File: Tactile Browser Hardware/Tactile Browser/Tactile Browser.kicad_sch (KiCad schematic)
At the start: 78 parts, among them SW1 SW_Push, SW10 SW_Push, SW11 SW_Push, SW12 SW_Push, SW13 SW_Push, SW14 SW_Push, SW15 SW_Push, SW16 SW_Push, SW17 SW_Push, SW18 SW_Push, SW19 SW_Push, SW2 SW_Push, SW20 SW_Push, SW3 SW_Push, SW4 SW_Push, SW5 SW_Push, SW6 SW_Push, SW7 SW_Push, SW8 SW_Push, SW9 SW_Push

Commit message: I2C
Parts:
- added I2C_bus: Conn_01x02_Pin, symbol Connector:Conn_01x02_Pin
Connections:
- net SDA: now reaches A1.23 (A4)
- net SDA: now also I2C_bus.1 (Pin_1)
- net SCL: now reaches A1.24 (A5)
- net SCL: now also I2C_bus.2 (Pin_2)
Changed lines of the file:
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@@
 		)
 	)
+	(global_label "SCL"
+		(shape input)
+		(at 254 71.12 270)
+		(fields_autoplaced yes)
+		(effects
+			(font
+				(size 1.27 1.27)
+			)
+			(justify right)
+		)
+		(property "Intersheetrefs" "${INTERSHEET_REFS}"
+			(at 254 77.6128 90)
+			(effects
+				(font
+					(size 1.27 1.27)
+				)
+				(justify right)
+				(hide yes)
+			)
+		)
+	)
 	(global_label "S2_in1"
 		(shape input)
@@
 		)
 	)
+	(global_label "SDA"
+		(shape input)
+		(at 256.54 71.12 270)
+		(fields_autoplaced yes)
+		(effects
+			(font
+				(size 1.27 1.27)
+			)
+			(justify right)
+		)
+		(property "Intersheetrefs" "${INTERSHEET_REFS}"
+			(at 256.54 77.6733 90)
+			(effects
+				(font
+					(size 1.27 1.27)
+				)
+				(justify right)
+				(hide yes)
+			)
+		)
+	)
 	(global_label "12V"
 		(shape input)
@@
 		)
 	)
+	(global_label "SDA"
+		(shape input)
+		(at 275.59 237.49 0)
+		(fields_autoplaced yes)
+		(effects
+			(font
+				(size 1.27 1.27)
+			)
+			(justify left)
+		)
+		(property "Intersheetrefs" "${INTERSHEET_REFS}"
+			(at 282.1433 237.49 0)
+			(effects
+				(font
+					(size 1.27 1.27)
+				)
+				(justify left)
+				(hide yes)
+			)
+		)
+	)
 	(global_label "S18_out2"
 		(shape input)
@@
 		)
 	)
+	(global_label "SCL"
+		(shape input)
+		(at 275.59 240.03 0)
+		(fields_autoplaced yes)
+		(effects
+			(font
+				(size 1.27 1.27)
+			)
+			(justify left)
+		)
+		(property "Intersheetrefs" "${INTERSHEET_REFS}"
+			(at 282.0828 240.03 0)
+			(effects
+				(font
+					(size 1.27 1.27)
+				)
+				(justify left)
+				(hide yes)
+			)
+		)
+	)
 	(global_label "5V"
 		(shape input)
@@
 					(unit 1)
 				)
+			)
+		)
+	)
+	(symbol
+		(lib_id "Connector:Conn_01x02_Pin")
+		(at 256.54 66.04 270)
+		(unit 1)
+		(exclude_from_sim no)
+		(in_bom yes)
+		(on_board yes)
+		(dnp no)
+		(fields_autoplaced yes)
+		(property "Reference" "I2C_bus"
+			(at 257.81 65.4049 90)
+			(effects
+				(font
+					(size 1.27 1.27)
+				)
+				(justify left)
+			)
+		)
+		(property "Value" "Conn_01x02_Pin"
+			(at 257.81 67.9449 90)
+			(effects
+				(font
+					(size 1.27 1.27)
+				)
+				(justify left)
+			)
+		)
+		(property "Footprint" ""
+			(at 256.54 66.04 0)
+			(effects
+				(font
+					(size 1.27 1.27)
+				)
+				(hide yes)
+			)
+		)
+		(property "Datasheet" "~"
+			(at 256.54 66.04 0)
+			(effects
+				(font
+					(size 1.27 1.27)
+				)
+				(hide yes)
+			)
+		)
+		(property "Description" "Generic connector, single row, 01x02, script generated"
+			(at 256.54 66.04 0)
+			(effects
+				(font
+					(size 1.27 1.27)
+				)
+				(hide yes)
+			)
+		)
+		(pin "1"
+		)
+		(pin "2"
+		)
+		(instances
+			(project ""
+				(path "/2e399075-89ae-469c-893b-1284214b820d"
+					(reference "I2C_bus")
+					(unit 1)
+				)

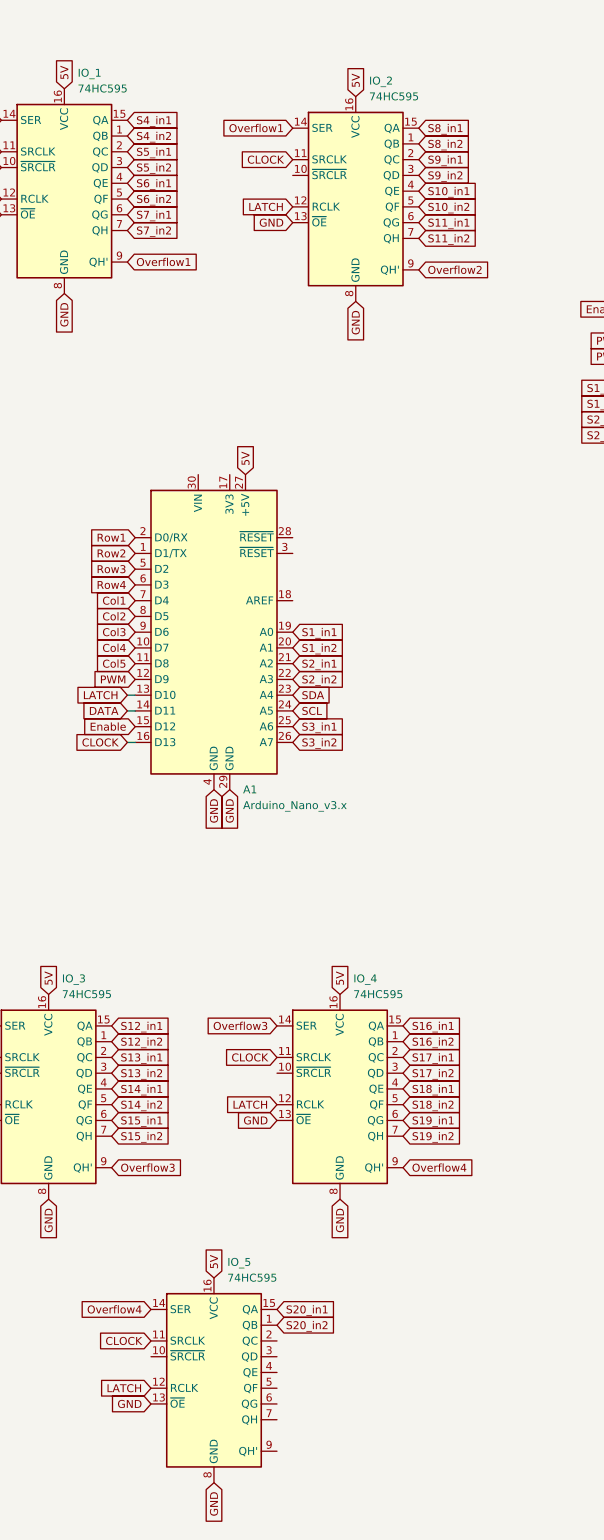
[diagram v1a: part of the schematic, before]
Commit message: moved all solenoids to 74hc595s
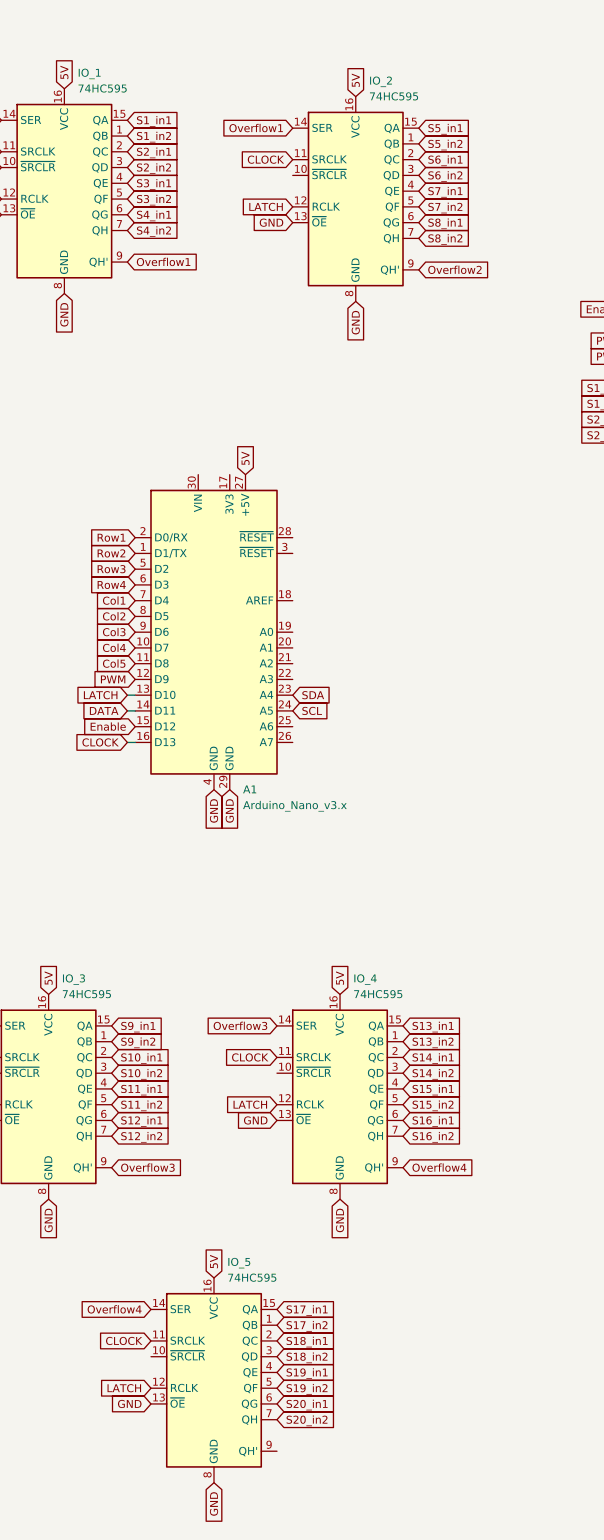
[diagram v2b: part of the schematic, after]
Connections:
- net S10_in1: now also IO_3.2 (QC); no longer IO_2.4 (QE)
- net S10_in2: now also IO_3.3 (QD); no longer IO_2.5 (QF)
- net S11_in1: now also IO_3.4 (QE); no longer IO_2.6 (QG)
- net S11_in2: now also IO_3.5 (QF); no longer IO_2.7 (QH)
- net S12_in1: now also IO_3.6 (QG); no longer IO_3.15 (QA)
- net S12_in2: now also IO_3.7 (QH); no longer IO_3.1 (QB)
- net S13_in1: now also IO_4.15 (QA); no longer IO_3.2 (QC)
- net S13_in2: now also IO_4.1 (QB); no longer IO_3.3 (QD)
- net S14_in1: now also IO_4.2 (QC); no longer IO_3.4 (QE)
- net S14_in2: now also IO_4.3 (QD); no longer IO_3.5 (QF)
- net S15_in1: now also IO_4.4 (QE); no longer IO_3.6 (QG)
- net S15_in2: now also IO_4.5 (QF); no longer IO_3.7 (QH)
- net S16_in1: now also IO_4.6 (QG); no longer IO_4.15 (QA)
- net S16_in2: now also IO_4.7 (QH); no longer IO_4.1 (QB)
- net S17_in1: now also IO_5.15 (QA); no longer IO_4.2 (QC)
- net S17_in2: now also IO_5.1 (QB); no longer IO_4.3 (QD)
- net S18_in1: now also IO_5.2 (QC); no longer IO_4.4 (QE)
- net S18_in2: now also IO_5.3 (QD); no longer IO_4.5 (QF)
- net S19_in1: now also IO_5.4 (QE); no longer IO_4.6 (QG)
- net S19_in2: now also IO_5.5 (QF); no longer IO_4.7 (QH)
- net S1_in1: now also IO_1.15 (QA); no longer A1.19 (A0)
- net S1_in2: now also IO_1.1 (QB); no longer A1.20 (A1)
- net S20_in1: now also IO_5.6 (QG); no longer IO_5.15 (QA)
- net S20_in2: now also IO_5.7 (QH); no longer IO_5.1 (QB)
- net S2_in1: now also IO_1.2 (QC); no longer A1.21 (A2)
- net S2_in2: now also IO_1.3 (QD); no longer A1.22 (A3)
- net S3_in1: now also IO_1.4 (QE); no longer A1.25 (A6)
- net S3_in2: now also IO_1.5 (QF); no longer A1.26 (A7)
- net S4_in1: now also IO_1.6 (QG); no longer IO_1.15 (QA)
- net S4_in2: now also IO_1.7 (QH); no longer IO_1.1 (QB)
- net S5_in1: now also IO_2.15 (QA); no longer IO_1.2 (QC)
- net S5_in2: now also IO_2.1 (QB); no longer IO_1.3 (QD)
- net S6_in1: now also IO_2.2 (QC); no longer IO_1.4 (QE)
- net S6_in2: now also IO_2.3 (QD); no longer IO_1.5 (QF)
- net S7_in1: now also IO_2.4 (QE); no longer IO_1.6 (QG)
- net S7_in2: now also IO_2.5 (QF); no longer IO_1.7 (QH)
- net S8_in1: now also IO_2.6 (QG); no longer IO_2.15 (QA)
- net S8_in2: now also IO_2.7 (QH); no longer IO_2.1 (QB)
- net S9_in1: now also IO_3.15 (QA); no longer IO_2.2 (QC)
- net S9_in2: now also IO_3.1 (QB); no longer IO_2.3 (QD)
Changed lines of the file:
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@@
 		)
 	)
-	(global_label "S8_in2"
+	(global_label "S5_in2"
 		(shape input)
 		(at 295.91 148.59 0)
@@
 		)
 	)
-	(global_label "S5_in2"
+	(global_label "S2_in2"
 		(shape input)
 		(at 248.92 152.4 0)
@@
 		)
 	)
-	(global_label "S11_in1"
+	(global_label "S8_in1"
 		(shape input)
 		(at 295.91 161.29 0)
@@
 		)
 		(property "Intersheetrefs" "${INTERSHEET_REFS}"
-			(at 306.4546 161.29 0)
+			(at 305.2451 161.29 0)
 			(effects
 				(font
@@
 		)
 	)
-	(global_label "S19_in1"
+	(global_label "S16_in1"
 		(shape input)
 		(at 293.37 306.07 0)
@@
 		)
 	)
-	(global_label "S12_in1"
+	(global_label "S9_in1"
 		(shape input)
 		(at 246.38 290.83 0)
@@
 		)
 		(property "Intersheetrefs" "${INTERSHEET_REFS}"
-			(at 256.9246 290.83 0)
+			(at 255.7151 290.83 0)
 			(effects
 				(font
@@
 		)
 	)
-	(global_label "S6_in2"
+	(global_label "S3_in2"
 		(shape input)
 		(at 248.92 157.48 0)
@@
 		)
 	)
-	(global_label "S14_in1"
+	(global_label "S11_in1"
 		(shape input)
 		(at 246.38 300.99 0)
@@
 		)
 	)
-	(global_label "S18_in2"
+	(global_label "S15_in2"
 		(shape input)
 		(at 293.37 303.53 0)
@@
 		)
 	)
-	(global_label "S20_in2"
+	(global_label "S17_in2"
 		(shape input)
 		(at 273.05 339.09 0)
@@
 		)
 	)
-	(global_label "S2_in2"
+	(global_label "S19_in2"
 		(shape input)
-		(at 275.59 234.95 0)
+		(at 273.05 349.25 0)
 		(fields_autoplaced yes)
 		(effects
@@
 		)
 		(property "Intersheetrefs" "${INTERSHEET_REFS}"
-			(at 284.9251 234.95 0)
+			(at 283.5946 349.25 0)
 			(effects
 				(font
@@
 		)
 	)
-	(global_label "S1_in1"
+	(global_label "S18_in1"
 		(shape input)
-		(at 275.59 227.33 0)
+		(at 273.05 341.63 0)
 		(fields_autoplaced yes)
 		(effects
@@
 		)
 		(property "Intersheetrefs" "${INTERSHEET_REFS}"
-			(at 284.9251 227.33 0)
+			(at 283.5946 341.63 0)
 			(effects
 				(font
@@
 		)
 	)
-	(global_label "S18_in1"
+	(global_label "S15_in1"
 		(shape input)
 		(at 293.37 300.99 0)
@@
 		)
 	)
-	(global_label "S9_in2"
+	(global_label "S6_in2"
 		(shape input)
 		(at 295.91 153.67 0)
@@
 		)
 	)
-	(global_label "S9_in1"
+	(global_label "S6_in1"
 		(shape input)
 		(at 295.91 151.13 0)
@@
 		)
 	)
-	(global_label "S13_in2"
+	(global_label "S10_in2"
 		(shape input)
 		(at 246.38 298.45 0)
@@
 		)
 	)
-	(global_label "S7_in2"
+	(global_label "S4_in2"
 		(shape input)
 		(at 248.92 162.56 0)
@@
 		)
 	)
-	(global_label "S7_in1"
+	(global_label "S4_in1"
 		(shape input)
 		(at 248.92 160.02 0)
@@
 		)
 	)
-	(global_label "S17_in2"
+	(global_label "S14_in2"
 		(shape input)
 		(at 293.37 298.45 0)
@@
 		)
 	)
-	(global_label "S13_in1"
+	(global_label "S10_in1"
 		(shape input)
 		(at 246.38 295.91 0)
@@
 		)
 	)
-	(global_label "S11_in2"
+	(global_label "S8_in2"
 		(shape input)
 		(at 295.91 163.83 0)
@@
 		)
 		(property "Intersheetrefs" "${INTERSHEET_REFS}"
-			(at 306.4546 163.83 0)
+			(at 305.2451 163.83 0)
 			(effects
 				(font
@@
 		)
 	)
-	(global_label "S10_in1"
+	(global_label "S7_in1"
 		(shape input)
 		(at 295.91 156.21 0)
@@
 		)
 		(property "Intersheetrefs" "${INTERSHEET_REFS}"
-			(at 306.4546 156.21 0)
+			(at 305.2451 156.21 0)
 			(effects
 				(font
@@
 		)
 	)
-	(global_label "S14_in2"
+	(global_label "S11_in2"
 		(shape input)
 		(at 246.38 303.53 0)
@@
 		)
 	)
-	(global_label "S8_in1"
+	(global_label "S5_in1"
 		(shape input)
 		(at 295.91 146.05 0)
@@
 		)
 	)
-	(global_label "S3_in2"
+	(global_label "S20_in2"
 		(shape input)
-		(at 275.59 245.11 0)
+		(at 273.05 354.33 0)
 		(fields_autoplaced yes)
 		(effects
@@
 		)
 		(property "Intersheetrefs" "${INTERSHEET_REFS}"
-			(at 284.9251 245.11 0)
+			(at 283.5946 354.33 0)
 			(effects
 				(font
@@
 		)
 	)
-	(global_label "S19_in2"
+	(global_label "S16_in2"
 		(shape input)
 		(at 293.37 308.61 0)
@@
 		)
 	)
-	(global_label "S5_in1"
+	(global_label "S2_in1"
 		(shape input)
 		(at 248.92 149.86 0)
@@
 		)
 	)
-	(global_label "S16_in1"
+	(global_label "S13_in1"
 		(shape input)
 		(at 293.37 290.83 0)
@@
 		)
 	)
-	(global_label "S20_in1"
+	(global_label "S17_in1"
 		(shape input)
 		(at 273.05 336.55 0)
@@
 		)
 	)
-	(global_label "S17_in1"
+	(global_label "S14_in1"
 		(shape input)
 		(at 293.37 295.91 0)
@@
 		)
 	)
-	(global_label "S15_in1"
+	(global_label "S12_in1"
 		(shape input)
 		(at 246.38 306.07 0)
@@
 		)
 	)
-	(global_label "S2_in1"
+	(global_label "S19_in1"
 		(shape input)
-		(at 275.59 232.41 0)
+		(at 273.05 346.71 0)
 		(fields_autoplaced yes)
 		(effects
@@
 		)
 		(property "Intersheetrefs" "${INTERSHEET_REFS}"
-			(at 284.9251 232.41 0)
+			(at 283.5946 346.71 0)
 			(effects
 				(font
@@
 		)
 	)
-	(global_label "S10_in2"
+	(global_label "S7_in2"
 		(shape input)
 		(at 295.91 158.75 0)
@@
 		)
 		(property "Intersheetrefs" "${INTERSHEET_REFS}"
-			(at 306.4546 158.75 0)
+			(at 305.2451 158.75 0)
 			(effects
 				(font
@@
 		)
 	)
-	(global_label "S3_in1"
+	(global_label "S20_in1"
 		(shape input)
-		(at 275.59 242.57 0)
+		(at 273.05 351.79 0)
 		(fields_autoplaced yes)
 		(effects
@@
 		)
 		(property "Intersheetrefs" "${INTERSHEET_REFS}"
-			(at 284.9251 242.57 0)
+			(at 283.5946 351.79 0)
 			(effects
 				(font
@@
 		)
 	)
-	(global_label "S12_in2"
+	(global_label "S9_in2"
 		(shape input)
 		(at 246.38 293.37 0)
@@
 		)
 		(property "Intersheetrefs" "${INTERSHEET_REFS}"
-			(at 256.9246 293.37 0)
+			(at 255.7151 293.37 0)
 			(effects
 				(font
@@
 		)
 	)
-	(global_label "S6_in1"
+	(global_label "S3_in1"
 		(shape input)
 		(at 248.92 154.94 0)
@@
 		)
 	)
-	(global_label "S15_in2"
+	(global_label "S12_in2"
 		(shape input)
 		(at 246.38 308.61 0)
@@
 		)
 	)
-	(global_label "S4_in1"
+	(global_label "S1_in1"
 		(shape input)
 		(at 248.92 144.78 0)
@@
 		)
 	)
-	(global_label "S16_in2"
+	(global_label "S13_in2"
 		(shape input)
 		(at 293.37 293.37 0)
@@
 		)
 	)
-	(global_label "S4_in2"
+	(global_label "S1_in2"
 		(shape input)
 		(at 248.92 147.32 0)
@@
 		)
 	)
-	(global_label "S1_in2"
+	(global_label "S18_in2"
 		(shape input)
-		(at 275.59 229.87 0)
+		(at 273.05 344.17 0)
 		(fields_autoplaced yes)
 		(effects
@@
 		)
 		(property "Intersheetrefs" "${INTERSHEET_REFS}"
-			(at 284.9251 229.87 0)
+			(at 283.5946 344.17 0)
 			(effects
 				(font
